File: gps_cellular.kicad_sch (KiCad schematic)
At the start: 47 parts, among them IC1 SGECL01-01-1000, J1 RECE.20279.001E.01, J2 RECE.20279.001E.01, J3 78800-0001, Q1 BC847CE6327HTSA1, Q2 BC847CE6327HTSA1, U2 LENA-R8001M10-00C

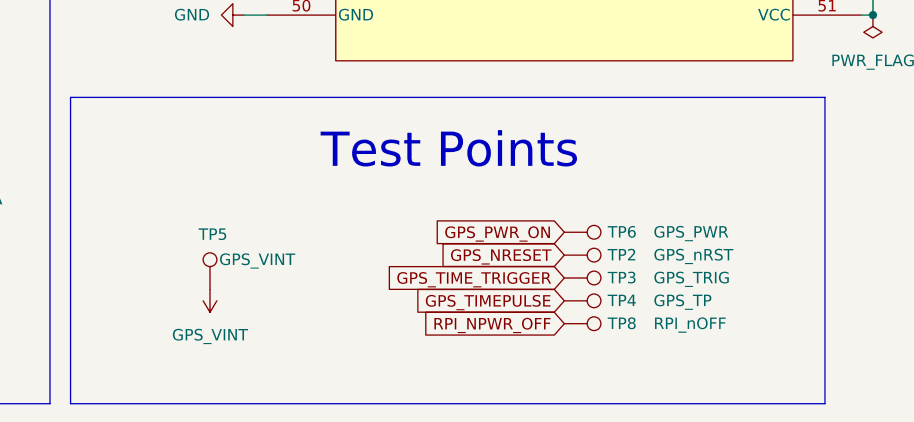
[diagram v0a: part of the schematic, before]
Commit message: Update silkscreen, add modem +5V via to regulator
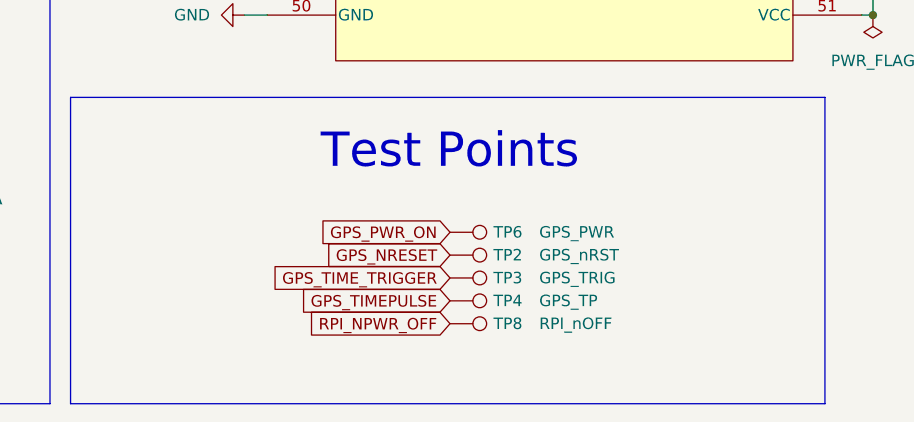
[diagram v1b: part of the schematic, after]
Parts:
- removed TP5: GPS_VINT, TestPoint:TestPoint_THTPad_D1.0mm_Drill0.5mm, symbol Connector:TestPoint
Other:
- moved on the sheet: TP2, TP3, TP4, TP6, TP8
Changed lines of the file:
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@@
 	(global_label "RPI_NPWR_OFF"
 		(shape input)
-		(at 144.78 186.69 180)
+		(at 132.08 186.69 180)
 		(fields_autoplaced yes)
 		(effects
@@
 		)
 		(property "Intersheetrefs" "${INTERSHEET_REFS}"
-			(at 127.8852 186.69 0)
+			(at 115.1852 186.69 0)
 			(effects
 				(font
@@
 	(global_label "GPS_TIMEPULSE"
 		(shape input)
-		(at 144.78 184.15 180)
+		(at 132.08 184.15 180)
 		(fields_autoplaced yes)
 		(effects
@@
 		)
 		(property "Intersheetrefs" "${INTERSHEET_REFS}"
-			(at 126.9178 184.15 0)
+			(at 114.2178 184.15 0)
 			(effects
 				(font
@@
 	(global_label "GPS_NRESET"
 		(shape input)
-		(at 144.78 179.07 180)
+		(at 132.08 179.07 180)
 		(fields_autoplaced yes)
 		(effects
@@
 		)
 		(property "Intersheetrefs" "${INTERSHEET_REFS}"
-			(at 130.0021 179.07 0)
+			(at 117.3021 179.07 0)
 			(effects
 				(font
@@
 	(global_label "GPS_TIME_TRIGGER"
 		(shape input)
-		(at 144.78 181.61 180)
+		(at 132.08 181.61 180)
 		(fields_autoplaced yes)
 		(effects
@@
 		)
 		(property "Intersheetrefs" "${INTERSHEET_REFS}"
-			(at 124.1359 181.61 0)
+			(at 111.4359 181.61 0)
 			(effects
 				(font
@@
 	(global_label "GPS_PWR_ON"
 		(shape input)
-		(at 144.78 176.53 180)
+		(at 132.08 176.53 180)
 		(fields_autoplaced yes)
 		(effects
@@
 		)
 		(property "Intersheetrefs" "${INTERSHEET_REFS}"
-			(at 129.4577 176.53 0)
+			(at 116.7577 176.53 0)
 			(effects
 				(font
@@
 	(symbol
 		(lib_id "Connector:TestPoint")
-		(at 144.78 181.61 270)
+		(at 132.08 181.61 270)
 		(unit 1)
 		(exclude_from_sim no)
@@
 		(dnp no)
 		(property "Reference" "TP3"
-			(at 149.606 181.61 90)
+			(at 136.906 181.61 90)
 			(effects
 				(font
@@
 		)
 		(property "Value" "GPS_TRIG"
-			(at 154.686 181.61 90)
+			(at 141.986 181.61 90)
 			(effects
 				(font
@@
 		)
 		(property "Footprint" "TestPoint:TestPoint_THTPad_D1.0mm_Drill0.5mm"
-			(at 144.78 186.69 0)
+			(at 132.08 186.69 0)
 			(effects
 				(font
@@
 		)
 		(property "Datasheet" "~"
-			(at 144.78 186.69 0)
+			(at 132.08 186.69 0)
 			(effects
 				(font
@@
 		)
 		(property "Description" "test point"
-			(at 144.78 181.61 0)
+			(at 132.08 181.61 0)
 			(effects
 				(font
@@
 		)
 		(property "MPN" ""
-			(at 144.78 181.61 0)
+			(at 132.08 181.61 0)
 			(effects
 				(font
@@
 	(symbol
 		(lib_id "Connector:TestPoint")
-		(at 144.78 179.07 270)
+		(at 132.08 179.07 270)
 		(unit 1)
 		(exclude_from_sim no)
@@
 		(dnp no)
 		(property "Reference" "TP2"
-			(at 149.606 179.07 90)
+			(at 136.906 179.07 90)
 			(effects
 				(font
@@
 		)
 		(property "Value" "GPS_nRST"
-			(at 154.686 179.07 90)
+			(at 141.986 179.07 90)
 			(effects
 				(font
@@
 		)
 		(property "Footprint" "TestPoint:TestPoint_THTPad_D1.0mm_Drill0.5mm"
-			(at 144.78 184.15 0)
+			(at 132.08 184.15 0)
 			(effects
 				(font
@@
 		)
 		(property "Datasheet" "~"
-			(at 144.78 184.15 0)
+			(at 132.08 184.15 0)
 			(effects
 				(font
@@
 		)
 		(property "Description" "test point"
-			(at 144.78 179.07 0)
+			(at 132.08 179.07 0)
 			(effects
 				(font
@@
 		)
 		(property "MPN" ""
-			(at 144.78 179.07 0)
+			(at 132.08 179.07 0)
 			(effects
 				(font
@@
 	(symbol
 		(lib_id "Connector:TestPoint")
-		(at 144.78 186.69 270)
+		(at 132.08 186.69 270)
 		(unit 1)
 		(exclude_from_sim no)
@@
 		(dnp no)
 		(property "Reference" "TP8"
-			(at 149.606 186.69 90)
+			(at 136.906 186.69 90)
 			(effects
 				(font
@@
 		)
 		(property "Value" "RPI_nOFF"
-			(at 154.686 186.69 90)
+			(at 141.986 186.69 90)
 			(effects
 				(font
@@
 		)
 		(property "Footprint" "TestPoint:TestPoint_THTPad_D1.0mm_Drill0.5mm"
-			(at 144.78 191.77 0)
+			(at 132.08 191.77 0)
 			(effects
 				(font
@@
 		)
 		(property "Datasheet" "~"
-			(at 144.78 191.77 0)
+			(at 132.08 191.77 0)
 			(effects
 				(font
@@
 		)
 		(property "Description" "test point"
-			(at 144.78 186.69 0)
+			(at 132.08 186.69 0)
 			(effects
 				(font
@@
 		)
 		(property "MPN" ""
-			(at 144.78 186.69 0)
+			(at 132.08 186.69 0)
 			(effects
 				(font
@@
 	(symbol
 		(lib_id "Connector:TestPoint")
-		(at 144.78 184.15 270)
+		(at 132.08 184.15 270)
 		(unit 1)
 		(exclude_from_sim no)
@@
 		(dnp no)
 		(property "Reference" "TP4"
-			(at 149.606 184.15 90)
+			(at 136.906 184.15 90)
 			(effects
 				(font
@@
 		)
 		(property "Value" "GPS_TP"
-			(at 154.686 184.15 90)
+			(at 141.986 184.15 90)
 			(effects
 				(font
@@
 		)
 		(property "Footprint" "TestPoint:TestPoint_THTPad_D1.0mm_Drill0.5mm"
-			(at 144.78 189.23 0)
+			(at 132.08 189.23 0)
 			(effects
 				(font
@@
 		)
 		(property "Datasheet" "~"
-			(at 144.78 189.23 0)
+			(at 132.08 189.23 0)
 			(effects
 				(font
@@
 		)
 		(property "Description" "test point"
-			(at 144.78 184.15 0)
+			(at 132.08 184.15 0)
 			(effects
 				(font
@@
 		)
 		(property "MPN" ""
-			(at 144.78 184.15 0)
+			(at 132.08 184.15 0)
 			(effects
 				(font
@@
 	)
 	(symbol
-		(lib_id "Connector:TestPoint")
-		(at 105.41 182.88 0)
-		(unit 1)
-		(exclude_from_sim no)
-		(in_bom no)
-		(on_board yes)
-		(dnp no)
-		(property "Reference" "TP5"
-			(at 104.14 176.784 0)
-			(effects
-				(font
-					(size 1.27 1.27)
-				)
-				(justify left)
-			)
-		)
-		(property "Value" "GPS_VINT"
-			(at 106.426 179.578 0)
-			(effects
-				(font
-					(size 1.27 1.27)
-				)
-				(justify left)
-			)
-		)
-		(property "Footprint" "TestPoint:TestPoint_THTPad_D1.0mm_Drill0.5mm"
-			(at 110.49 182.88 0)
-			(effects
-				(font
-					(size 1.27 1.27)
-				)
-				(hide yes)
-			)
-		)
-		(property "Datasheet" "~"
-			(at 110.49 182.88 0)
-			(effects
-				(font
-					(size 1.27 1.27)
-				)
-				(hide yes)
-			)
-		)
-		(property "Description" "test point"
-			(at 105.41 182.88 0)
-			(effects
-				(font
-					(size 1.27 1.27)
-				)
-				(hide yes)
-			)
-		)
-		(property "MPN" ""
-			(at 105.41 182.88 0)
-			(effects
-				(font
-					(size 1.27 1.27)
-				)
-				(hide yes)
-			)
-		)
-		(pin "1"
-		)
-		(instances
-			(project "hw"
-				(path "/37690768-e2be-4a37-b8f7-45d5da107609/50f7e6f4-74ef-4126-87be-18568f5f475d"
-					(reference "TP5")
-					(unit 1)
-				)
-			)
-		)
-	)
-	(symbol
 		(lib_id "power:GND")
 		(at 96.52 116.84 180)
@@
 	)
 	(symbol
-		(lib_id "power:VCC")
-		(at 105.41 182.88 180)
-		(unit 1)
-		(exclude_from_sim no)
-		(in_bom yes)
-		(on_board yes)
-		(dnp no)
-		(fields_autoplaced yes)
-		(property "Reference" "#PWR0114"
-			(at 105.41 179.07 0)
-			(effects
-				(font
-					(size 1.27 1.27)
-				)
-				(hide yes)
-			)
-		)
-		(property "Value" "GPS_VINT"
-			(at 105.41 187.96 0)
-			(effects
-				(font
-					(size 1.27 1.27)
-				)
-			)
-		)
-		(property "Footprint" ""
-			(at 105.41 182.88 0)
-			(effects
-				(font
-					(size 1.27 1.27)
-				)
-				(hide yes)
-			)
-		)
-		(property "Datasheet" ""
-			(at 105.41 182.88 0)
-			(effects
-				(font
-					(size 1.27 1.27)
-				)
-				(hide yes)
-			)
-		)
-		(property "Description" "Power symbol creates a global label with name \"VCC\""
-			(at 105.41 182.88 0)
-			(effects
-				(font
-					(size 1.27 1.27)
-				)
-				(hide yes)
-			)
-		)
-		(pin "1"
-		)
-		(instances
-			(project "hw"
-				(path "/37690768-e2be-4a37-b8f7-45d5da107609/50f7e6f4-74ef-4126-87be-18568f5f475d"
-					(reference "#PWR0114")
-					(unit 1)
-				)
-			)
-		)
-	)
-	(symbol
 		(lib_id "power:GND")
 		(at 63.5 100.33 180)
@@
 	(symbol
 		(lib_id "Connector:TestPoint")
-		(at 144.78 176.53 270)
+		(at 132.08 176.53 270)
 		(unit 1)
 		(exclude_from_sim no)
@@
 		(dnp no)
 		(property "Reference" "TP6"
-			(at 149.606 176.53 90)
+			(at 136.906 176.53 90)
 			(effects
 				(font
@@
 		)
 		(property "Value" "GPS_PWR"
-			(at 154.686 176.53 90)
+			(at 141.986 176.53 90)
 			(effects
 				(font
@@
 		)
 		(property "Footprint" "TestPoint:TestPoint_THTPad_D1.0mm_Drill0.5mm"
-			(at 144.78 181.61 0)
+			(at 132.08 181.61 0)
 			(effects
 				(font
@@
 		)
 		(property "Datasheet" "~"
-			(at 144.78 181.61 0)
+			(at 132.08 181.61 0)
 			(effects
 				(font
@@
 		)
 		(property "Description" "test point"
-			(at 144.78 176.53 0)
+			(at 132.08 176.53 0)
 			(effects
 				(font
@@
 		)
 		(property "MPN" ""
-			(at 144.78 176.53 0)
+			(at 132.08 176.53 0)
 			(effects
 				(font

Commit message: New structure for holding parts, symbols, and footprints
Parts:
- C69: footprint T520B337M006ATE040:CAPMP3.7X2.8_2N_KEM -> CivicAlert:T520B337M006ATE040
- CELL1, GPS1: footprint LTST-C193TBKT-5A:LED_LTST-C_LTO -> CivicAlert:LTST-C193TBKT-5A
- CR1, CR2, CR3, CR4: footprint PESD0402-140:PESD0402-140_LTF -> CivicAlert:PESD0402-140_LTF
- FL1: footprint BLM18EG221SN1D:BEADC1608X95N -> CivicAlert:BLM18EG221SN1D
- IC1: footprint SGECL01-01-1000:SON127P600X500X80-9N-D -> CivicAlert:SGECL01-01-1000
- J1, J2: footprint RECE.20279.001E.01:CON3_RECE.20279.001E.01_TAL -> CivicAlert:RECE.20279.001E.01
- J3: footprint 0788000001:MOLEX_0788000001 -> CivicAlert:0788000001
- Q1, Q2: footprint BC847CE6327HTSA1:PG-SOT23-3-1_INF -> CivicAlert:BC847CE6327HTSA1
- U2: footprint LENA-R8001M10-00C:MOD100_LENA-R8_UBL -> CivicAlert:LENA-R8001M10-00C
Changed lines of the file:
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@@
 			)
 		)
-		(property "Footprint" "PESD0402-140:PESD0402-140_LTF"
+		(property "Footprint" "CivicAlert:PESD0402-140_LTF"
 			(at 219.71 67.31 0)
 			(effects
@@
 			)
 		)
-		(property "Footprint" "BLM18EG221SN1D:BEADC1608X95N"
+		(property "Footprint" "CivicAlert:BLM18EG221SN1D"
 			(at 196.85 149.86 0)
 			(effects
@@
 			)
 		)
-		(property "Footprint" "PESD0402-140:PESD0402-140_LTF"
+		(property "Footprint" "CivicAlert:PESD0402-140_LTF"
 			(at 217.17 80.01 0)
 			(effects
@@
 			)
 		)
-		(property "Footprint" "T520B337M006ATE040:CAPMP3.7X2.8_2N_KEM"
+		(property "Footprint" "CivicAlert:T520B337M006ATE040"
 			(at 257.81 149.86 0)
 			(effects
@@
 			)
 		)
-		(property "Footprint" "LTST-C193TBKT-5A:LED_LTST-C_LTO"
+		(property "Footprint" "CivicAlert:LTST-C193TBKT-5A"
 			(at 53.34 39.37 0)
 			(effects
@@
 			)
 		)
-		(property "Footprint" "0788000001:MOLEX_0788000001"
+		(property "Footprint" "CivicAlert:0788000001"
 			(at 238.76 40.64 0)
 			(effects
@@
 			)
 		)
-		(property "Footprint" "BC847CE6327HTSA1:PG-SOT23-3-1_INF"
+		(property "Footprint" "CivicAlert:BC847CE6327HTSA1"
 			(at 48.26 180.34 0)
 			(effects
@@
 			)
 		)
-		(property "Footprint" "RECE.20279.001E.01:CON3_RECE.20279.001E.01_TAL"
+		(property "Footprint" "CivicAlert:RECE.20279.001E.01"
 			(at 60.96 106.68 0)
 			(effects
@@
 			)
 		)
-		(property "Footprint" "SGECL01-01-1000:SON127P600X500X80-9N-D"
+		(property "Footprint" "CivicAlert:SGECL01-01-1000"
 			(at 262.89 199.06 0)
 			(effects
@@
 			)
 		)
-		(property "Footprint" "LENA-R8001M10-00C:MOD100_LENA-R8_UBL"
+		(property "Footprint" "CivicAlert:LENA-R8001M10-00C"
 			(at 111.76 27.94 0)
 			(effects
@@
 			)
 		)
-		(property "Footprint" "RECE.20279.001E.01:CON3_RECE.20279.001E.01_TAL"
+		(property "Footprint" "CivicAlert:RECE.20279.001E.01"
 			(at 210.82 142.24 0)
 			(effects
@@
 			)
 		)
-		(property "Footprint" "PESD0402-140:PESD0402-140_LTF"
+		(property "Footprint" "CivicAlert:PESD0402-140_LTF"
 			(at 260.35 53.34 0)
 			(effects
@@
 			)
 		)
-		(property "Footprint" "BC847CE6327HTSA1:PG-SOT23-3-1_INF"
+		(property "Footprint" "CivicAlert:BC847CE6327HTSA1"
 			(at 45.72 54.61 0)
 			(effects
@@
 			)
 		)
-		(property "Footprint" "PESD0402-140:PESD0402-140_LTF"
+		(property "Footprint" "CivicAlert:PESD0402-140_LTF"
 			(at 222.25 54.61 0)
 			(effects
@@
 			)
 		)
-		(property "Footprint" "LTST-C193TBKT-5A:LED_LTST-C_LTO"
+		(property "Footprint" "CivicAlert:LTST-C193TBKT-5A"
 			(at 55.88 165.1 0)
 			(effects

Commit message: Update for RevB
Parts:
- removed CELL1, GPS1: LTST-C193TBKT-5A, CivicAlert:LTST-C193TBKT-5A, symbol LTST-C193TBKT-5A:LTST-C193TBKT-5A
- removed Q1, Q2: BC847CE6327HTSA1, CivicAlert:BC847CE6327HTSA1, symbol BC847CE6327HTSA1:BC847CE6327HTSA1
- removed TP2: GPS_nRST, TestPoint:TestPoint_THTPad_D1.0mm_Drill0.5mm, symbol Connector:TestPoint
- removed TP4: GPS_TP, TestPoint:TestPoint_THTPad_D1.0mm_Drill0.5mm, symbol Connector:TestPoint
- removed TP8: RPI_nOFF, TestPoint:TestPoint_THTPad_D1.0mm_Drill0.5mm, symbol Connector:TestPoint
- added CELL1, GPS1: LTST-C190KGKT, CivicAlert:LTST-C190KGKT, symbol LTST-C190KGKT:LTST-C190KGKT
- added Q3, Q4: MMBT3904LT3G, CivicAlert:MMBT3904LT3G, symbol MMBT3904LT3G:BC847CE6327HTSA1
- C100: renamed from C12; MANUFACTURER Murata -> (none); MPN GRT1555C1H1R5CA02J -> (none); Manufacturer (none) -> Murata
- C101: renamed from C11; MANUFACTURER Murata -> (none); MPN GJM1555C1HR50WB01 -> (none); Manufacturer (none) -> Murata
- C102: renamed from C69; MANUFACTURER KEMET -> (none); MPN T520B337M006ATE040 -> (none); Manufacturer (none) -> KEMET
- C103: renamed from C4; MANUFACTURER Murata -> (none); MPN GRT1555C1H8R2DA02D -> (none); Manufacturer (none) -> Murata
- C104: renamed from C5; MANUFACTURER Murata -> (none); MPN GRT1555C1H150JA02J -> (none); Manufacturer (none) -> Murata
- C105: renamed from C6; MANUFACTURER Murata -> (none); MPN GRT1555C1H820FA02D -> (none); Manufacturer (none) -> Murata
- C106: renamed from C7; MANUFACTURER Murata -> (none); MPN GCM155R71H103KA55D -> (none); Manufacturer (none) -> Murata
- C107: renamed from C8; value 100n -> 0.1u; MANUFACTURER Murata -> (none); MPN GRT155R71H104KE01D -> (none); Manufacturer (none) -> Murata
- C92: renamed from C10; value 100n -> 0.1u; MANUFACTURER Murata -> (none); MPN GRT155R71H104KE01D -> (none); Manufacturer (none) -> Murata
- C93: renamed from C3; value 100n -> 0.1u; MANUFACTURER Murata -> (none); MPN GRT155R71H104KE01D -> (none); Manufacturer (none) -> Murata
- C94: renamed from C13; value 100n -> 0.1u; MANUFACTURER Murata -> (none); MPN GRT155R71H104KE01D -> (none); Manufacturer (none) -> Murata
- C95: renamed from C14; MANUFACTURER Murata -> (none); MPN GRT1555C1H470JA02J -> (none); Manufacturer (none) -> Murata
- C96: renamed from C15; MANUFACTURER Murata -> (none); MPN GRT1555C1H470JA02J -> (none); Manufacturer (none) -> Murata
- C97: renamed from C16; MANUFACTURER Murata -> (none); MPN GRT1555C1H470JA02J -> (none); Manufacturer (none) -> Murata
- C98: renamed from C17; MANUFACTURER Murata -> (none); MPN GRT1555C1H470JA02J -> (none); Manufacturer (none) -> Murata
- C99: renamed from C18; value 100n -> 0.1u; MANUFACTURER Murata -> (none); MPN GRT155R71H104KE01D -> (none); Manufacturer (none) -> Murata
- CELL2: renamed from J1; MANUFACTURER Taoglas -> (none); MPN RECE.20279.001E.01 -> (none); Manufacturer (none) -> Taoglas
- CR2: renamed from CR4; MANUFACTURER Littelfuse -> (none); MPN PESD0402-140 -> (none); Manufacturer (none) -> Littelfuse
- CR3: renamed from CR1; MANUFACTURER Littelfuse -> (none); MPN PESD0402-140 -> (none); Manufacturer (none) -> Littelfuse
- CR4: renamed from CR2; MANUFACTURER Littelfuse -> (none); MPN PESD0402-140 -> (none); Manufacturer (none) -> Littelfuse
- CR5: renamed from CR3; MANUFACTURER Littelfuse -> (none); MPN PESD0402-140 -> (none); Manufacturer (none) -> Littelfuse
- FL2: renamed from FL1; MANUFACTURER Murata -> (none); MPN BLM18EG221SN1D -> (none); Manufacturer (none) -> Murata
- GNSS1: renamed from J2; MANUFACTURER Taoglas -> (none); MPN RECE.20279.001E.01 -> (none); Manufacturer (none) -> Taoglas
- J2: renamed from J3; MANUFACTURER Molex -> (none); MAXIMUM_PACKAGE_HEIGHT 1.6 mm -> (none); MPN 78800-0001 -> (none); Manufacturer (none) -> Molex; PARTREV A -> (none); STANDARD Manufacturer Recommendations -> (none)
- L3: renamed from L4; MANUFACTURER Murata -> (none); MPN LQW15ANR12J00 -> (none); Manufacturer (none) -> Murata
- L4: renamed from L3; MANUFACTURER Murata -> (none); MPN LQG15WZ3N4S02D -> (none); Manufacturer (none) -> Murata
- L5: renamed from L1; MANUFACTURER Murata -> (none); MPN LQG15HH2N7B02 -> (none); Manufacturer (none) -> Murata
- L6: renamed from L2; MANUFACTURER Murata -> (none); MPN LQG15HH1N2B02 -> (none); Manufacturer (none) -> Murata
- R46: renamed from R23; value 500 -> 300
- R50: renamed from R25; value 500 -> 300
- TP2: renamed from TP3; value GPS_TRIG -> GPS_VINT
- U12: renamed from U2; MANUFACTURER u-blox -> (none); MPN LENA-R8001M10-00C -> (none); Manufacturer (none) -> u-blox
- renumbered IC1 to IC5, R22 to R47, R24 to R48, R4 to R49, R20 to R51, R42 to R52, TP6 to TP1
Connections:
- net GND: now also Q3.2, Q4.2
- net GPS_TIME_TRIGGER: no longer TP2.1
- net GPS_VINT: now also TP2.1
- net at R50.1: now also GPS1.A
- net at R46.1: now also CELL1.A
- net at R51.2, R52.1: now also Q4.1
- net at R47.2, R48.1: now also Q3.1
- net ANTENNA_VCC renamed VCC_GPS_ANT
- net GPS_VCC renamed VCC_CELL_GPS
- new net: CELL1.C, Q3.3
- new net: GPS1.C, Q4.3
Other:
- moved on the sheet: R46, R47, R48, R50, R51, R52, TP2

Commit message: Finalize RevB
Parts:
- C100: MPN (none) -> GRT1555C1H1R5CA02J
- C101: MPN (none) -> GJM1555C1HR50WB01D
- C102: MPN (none) -> T520B337M006ATE040
- C103: MPN (none) -> GRM1555C1E8R2CA01D
- C104: MPN (none) -> GRT1555C1H150JA02J
- C105: MPN (none) -> GRT1555C1H820FA02D
- C106: MPN (none) -> GCM155R71H103KA55D
- C107, C92, C93, C94, C99: MPN (none) -> GRM155R71C104KA88J
- C95, C96, C97, C98: MPN (none) -> GRT1555C1H470JA02J
- CELL1, GPS1: MPN (none) -> LTST-C190KGKT
- CELL2, GNSS1: MPN (none) -> RECE.20279.001E.01
- CR2, CR3, CR4, CR5: MPN (none) -> PESD0402-140
- FL2: MPN (none) -> BLM18EG221SN1D
- IC5: Height 0.8 -> (none); Manufacturer_Name Soracom -> (none); Manufacturer_Part_Number SGECL01-01-1000 -> (none); Mouser Part Number 432-SGECL01-01-1000 -> (none); Mouser Price/Stock https://www.mouser.co.uk/ProductDetail/Soracom/SGECL01-01-1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 -> (none)
- J2: MPN (none) -> 0788000001
- L3: MPN (none) -> LQW15ANR12J00
- L4: MPN (none) -> LQG15WZ3N4S02D
- L5: MPN (none) -> LQG15HS2N7B02D
- L6: MPN (none) -> LQG15HS1N2B02D
- Q3, Q4: MPN (none) -> BC847CE6327HTSA1
- U12: MPN (none) -> LENA-R8001M10-00C

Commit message: Add fiducials
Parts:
- added FID1, FID2, FID3, FID4, FID5, FID6: Fiducial, Fiducial:Fiducial_1mm_Mask3mm, symbol Mechanical:Fiducial

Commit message: Updates for Rev. C
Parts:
- removed FID1, FID2, FID3, FID4, FID5, FID6: Fiducial, Fiducial:Fiducial_1mm_Mask3mm, symbol Mechanical:Fiducial
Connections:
- net GPS_VINT: now also U12.100 (VBCKP_GNSS)
- no-connect marks 26 -> 25

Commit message: Update RevC design
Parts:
- R46, R50: value 300 -> 330
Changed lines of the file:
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@@
 			)
 		)
-		(property "Value" "300"
+		(property "Value" "330"
 			(at 62.23 162.5599 0)
 			(effects
@@
 			)
 		)
-		(property "Value" "300"
+		(property "Value" "330"
 			(at 60.96 34.2899 0)
 			(effects
